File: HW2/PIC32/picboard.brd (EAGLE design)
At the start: 50 x 50 mm, 22 parts, among them J1 USB

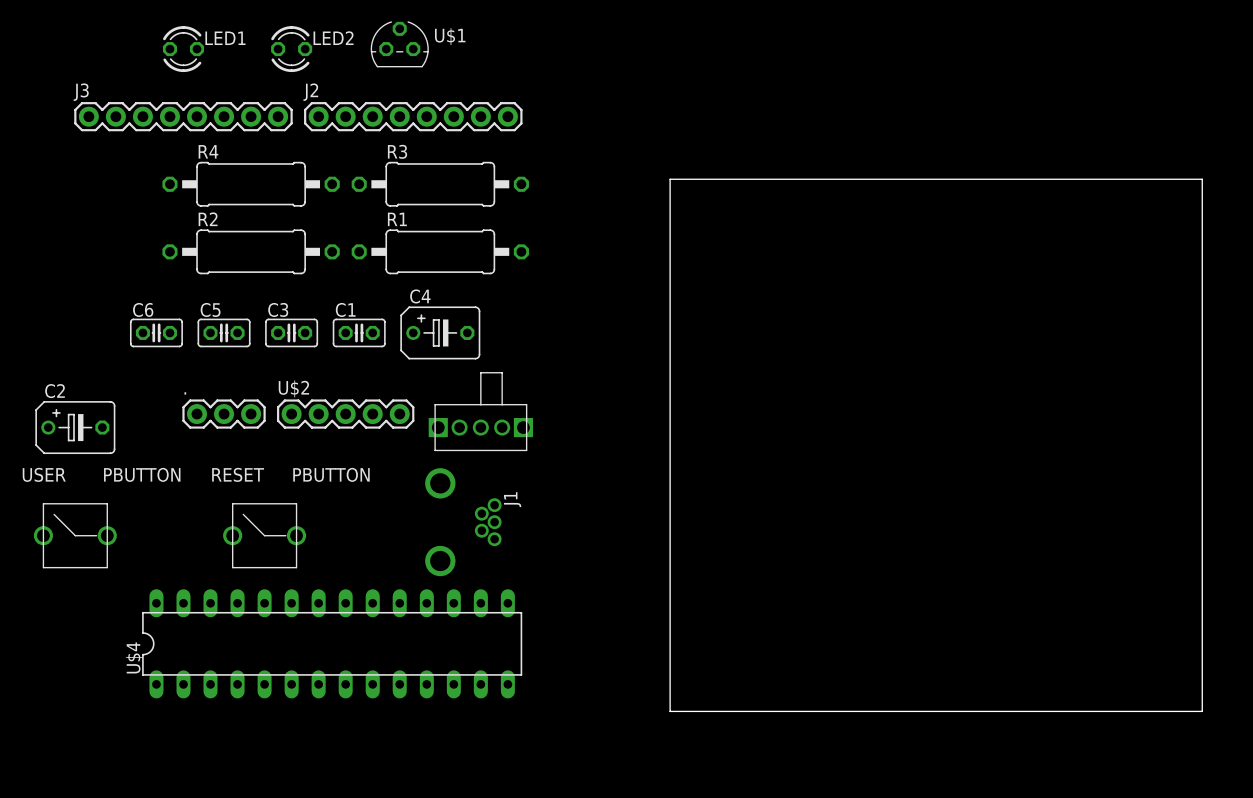
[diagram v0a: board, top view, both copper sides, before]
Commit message: finished PCB .brd layout. Still need to error check
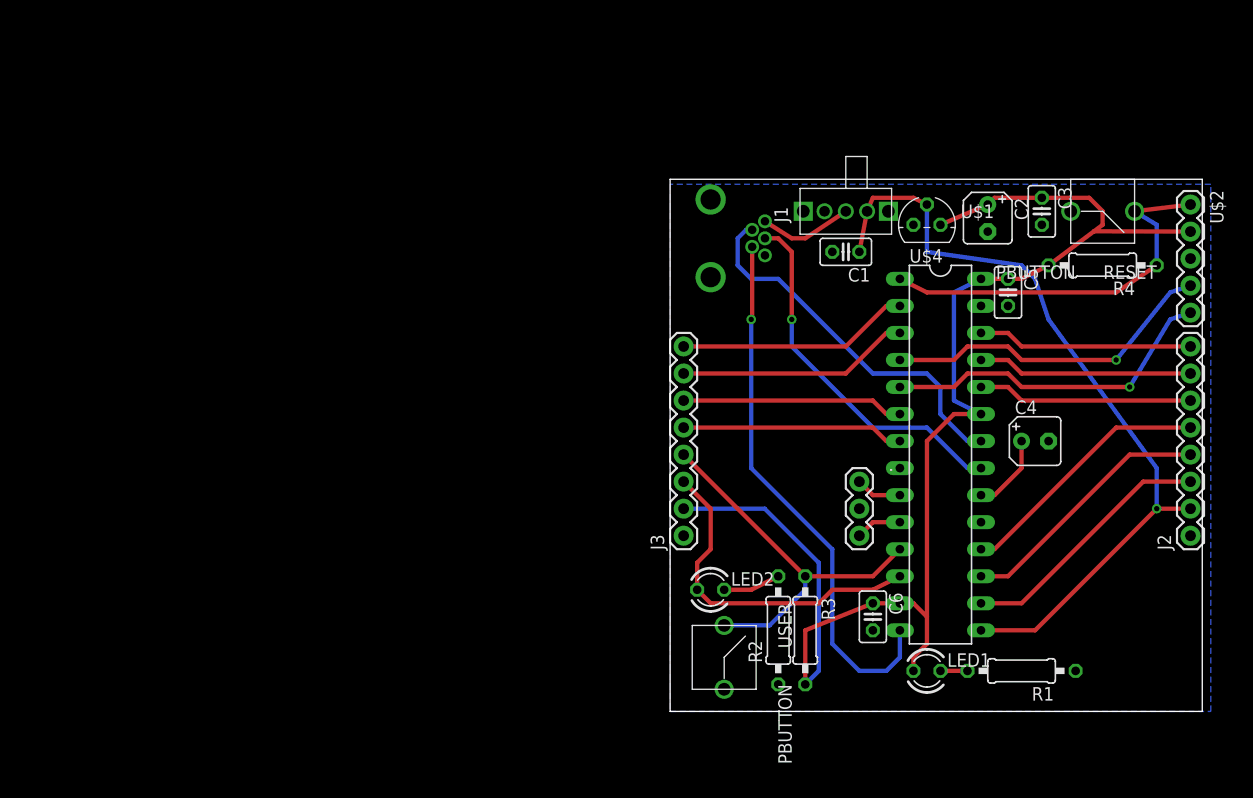
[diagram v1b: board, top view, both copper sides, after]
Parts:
- .: value OSCIL -> 8MHz
- C2, C4: device PIC32:B45181B -> PIC32:B45181A
- R1, R2, R3, R4: device PIC32:0411/15 -> PIC32:0207/10
- moved LED1 91.1 mm to (24.1, 3.81)
- moved J2 90.9 mm to (48.9, 16.5), turned to 90 degrees
- moved C2 88.0 mm to (29.8, 46.4), turned to 270 degrees
- moved U$2 86.7 mm to (48.9, 47.6), turned to 270 degrees
- moved RESET 84.4 mm to (40.6, 47.0), turned to 180 degrees
- moved R4 80.4 mm to (40.6, 41.9), turned to 180 degrees
- moved C5 73.8 mm to (31.8, 39.4), turned to 270 degrees
- moved C6 72.4 mm to (19.1, 8.89), turned to 270 degrees
- moved C3 71.4 mm to (34.9, 47.0), turned to 270 degrees
- moved J3 68.4 mm to (1.27, 16.5), turned to 90 degrees
- moved R1 67.3 mm to (33.0, 3.81), turned to 180 degrees
- moved LED2 64.3 mm to (3.81, 11.4)
- moved . 62.6 mm to (17.8, 21.6), turned to 270 degrees
- moved USER 62.0 mm to (5.08, 5.08), turned to 270 degrees
- moved R2 61.0 mm to (10.2, 7.62), turned to 90 degrees
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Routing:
- net +3V3: track 0.00 -> 128.1 mm
- net +5V: track 0.00 -> 75.2 mm, vias 0 -> 1
- net USBID: track 0.00 -> 51.0 mm, vias 0 -> 1
- net MCLR: track 0.00 -> 36.7 mm
- net USER/B4: track 0.00 -> 36.4 mm
- net D-: track 0.00 -> 35.4 mm
- net D+: track 0.00 -> 34.5 mm, vias 0 -> 1
- net LED/A4: track 0.00 -> 32.1 mm
- net PGC: track 0.00 -> 32.1 mm, vias 0 -> 1
- net PGD: track 0.00 -> 31.5 mm, vias 0 -> 1
- net B9: track 0.00 -> 24.4 mm
- net B8: track 0.00 -> 24.4 mm
- net B7: track 0.00 -> 24.4 mm
- net A1: track 0.00 -> 21.9 mm
- net A0: track 0.00 -> 21.9 mm
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- added copper zone on layer 16, net GND
